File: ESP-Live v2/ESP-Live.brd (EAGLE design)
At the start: 64.8 x 30.5 mm, 34 parts, among them CN1 USBSMD, IC2 AP2210K-3.3TRG1, IC3 ESP-12F, Y1 RESONATORSMD

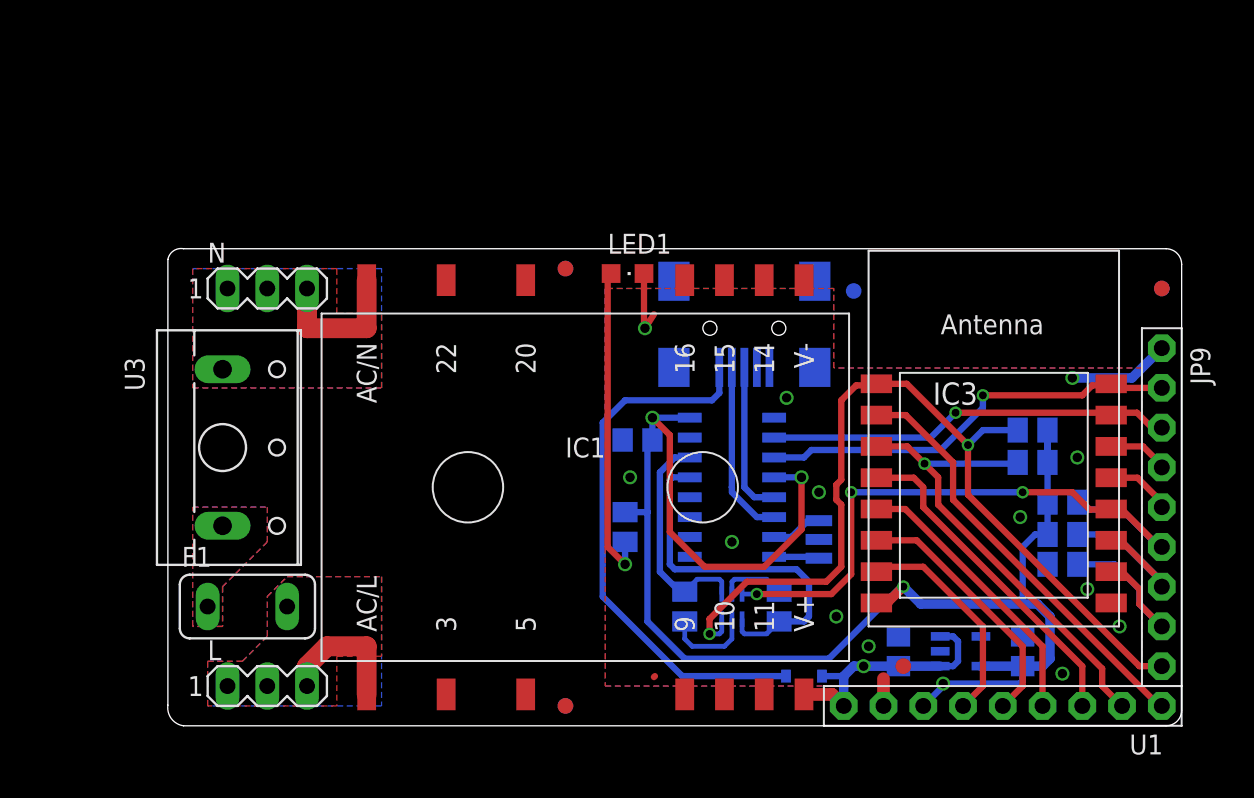
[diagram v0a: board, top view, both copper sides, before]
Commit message: with batery charger
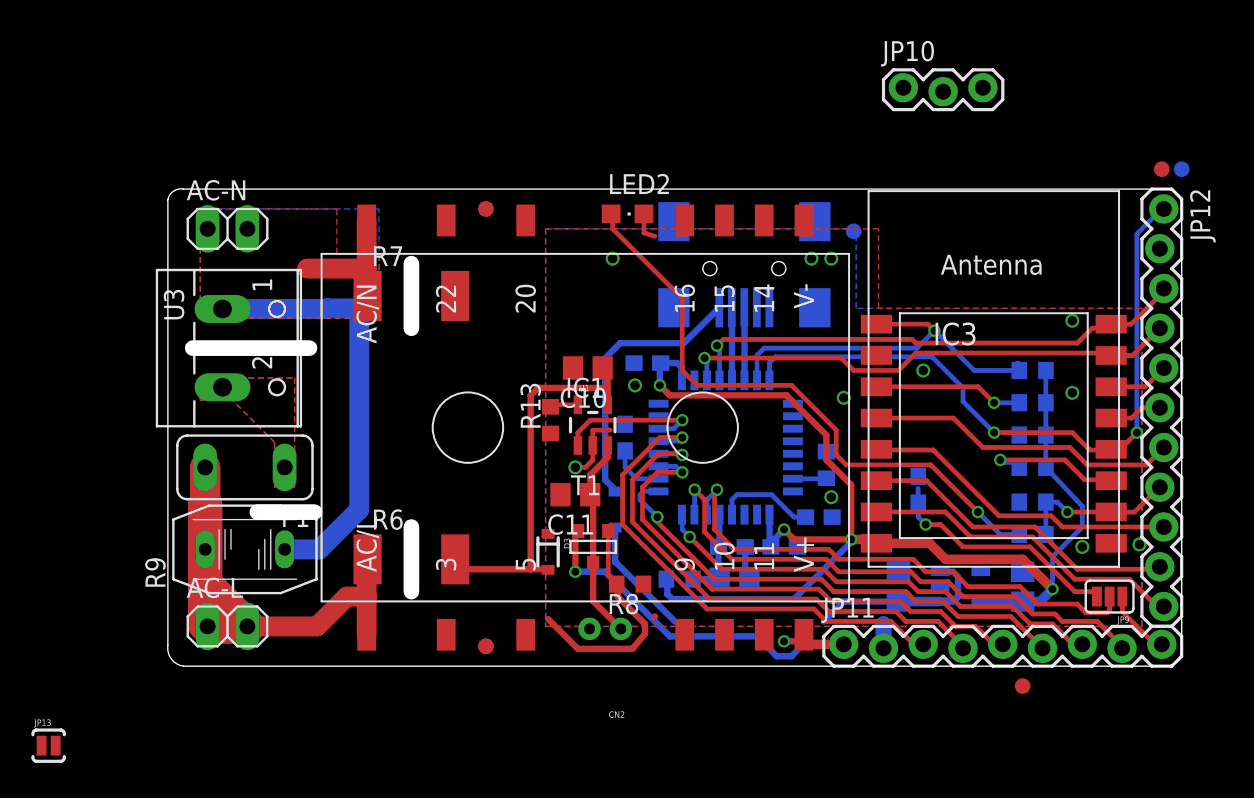
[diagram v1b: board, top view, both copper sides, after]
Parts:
- removed L, N: (no value), con-lstb:MA03-1
- removed LED1: (no value), adafruit:CHIPLED_0805
- removed U$2: MMDT3904, SparkFun:SOT363
- removed Y1: RESONATORSMD, SparkFun:RESONATOR-SMD
- added AC-L, AC-N: (no value), pinhead:1X02
- added C10, C11: 4.7uF, rcl:C0805
- added C4, C5, C7, C8, C9: 100nF, rcl:C0603
- added C6: 1uF, rcl:C0805
- added CN2: (no value), SparkFun:JST-2-PTH-NS
- added D3: PMEG3010EJ, SparkFun:SOD-323
- added JP10: (no value), SparkFun:1X03_LOCK
- added JP11: M09LOCK, SparkFun:1X09_LOCK
- added JP12: M11LOCK, SparkFun:1X11_LOCK
- added JP13: (no value), SparkFun:SJ_2S-NO
- added LED2: (no value), adafruit:CHIPLED_0805
- added R10: BEAD, rcl:R0603
- added R11: 10k, rcl:R0603
- added R12: 1k, rcl:R0603
- added R13: 2k, rcl:R0603
- added R9: 275VAC, varistor:P593
- added T1: (no value), zetex:SOT-23
- C3: value 0.1uF -> 100nF; device rcl:C0805 -> rcl:C0603
- JP9: value (none) -> CH1_CAP; device adafruit:1X09-BIG -> SparkFun:SJ_3_PASTE1&2
- R1, R2, R3, R4, R5: device rcl:M0805 -> rcl:R0603
- R6, R7: value 10k -> 0*; device rcl:M0805 -> rcl:R2512
- R8: value 1k -> 100k; device rcl:M0805 -> rcl:R0603
- U$1: value CH340G -> STM32F042K; device usb-serial:SOIC16 -> stm32:LQFP32
- U1: value (none) -> MCP73831; device adafruit:1X09-BIG -> SparkFun:SOT23-5
- U3: device con-wago-500:W237-113 -> con-wago-500:W237-102
- moved U1 31.7 mm to (27.1, 19.2), turned to 0 degrees
- moved R7 26.4 mm to (15.6, 27.5), flipped to the top, turned to 0 degrees
- moved R6 23.7 mm to (15.6, 10.6), flipped to the top, turned to 0 degrees
- moved D1 16.1 mm to (28.6, 13.8), turned to 90 degrees
- moved C3 11.6 mm to (39.4, 11.4), turned to 180 degrees
- moved F1 8.89 mm to (4.92, 16.5), turned to 180 degrees
- moved JP5 7.73 mm to (64.8, 35.6)
- moved JP4 7.73 mm to (54.6, 2.54)
- moved JP3 7.62 mm to (63.5, 35.6)
- moved JP9 6.62 mm to (60.2, 8.26), turned to 180 degrees
- moved JP2 6.35 mm to (20.3, 33.0)
- moved JP6 6.35 mm to (20.3, 33.0)
- moved JP1 6.35 mm to (20.3, 5.08)
- moved JP8 6.35 mm to (20.3, 5.08)
- moved U3 6.35 mm to (4.76, 24.1)
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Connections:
- removed net N$15: R7.1, U$1.14, U$2.1
- removed net N$16: CN1.D-, U$1.6
- removed net N$21: U$1.7, Y1.1
- removed net N$22: U$1.8, Y1.3
- removed net N$4: LED1.A, R8.2
- removed net N$8: R7.2, U$2.5
- new net BATT_STAT: U$1.14, U1.1
- new net BOOT0: JP10.3, R11.1, U$1.31
- new net L: AC-L.1, AC-L.2, F1.2, IC1.AC/L, R6.1, R9.1
- new net N: AC-N.1, AC-N.2, IC1.AC/N, R7.1, R9.2, U3.1
- new net N$13: C11.1, CN2.1, T1.1, U1.3
- new net N$6: CN1.D-, U$1.21
- new net N$7: CN1.D+, U$1.22
- new net SPI1_MISO: JP11.4, U$1.12
- new net SPI1_MOSI: JP11.3, U$1.13
- new net SPI1_SCK: JP11.5, U$1.11
- new net STM_NRST: C7.1, JP10.1, U$1.4
- new net TIM2_CH1: JP9.2, U$1.6
- new net TIM2_CH1_OPT: JP11.9, JP9.1
- new net TIM2_CH2: JP11.8, U$1.7
- new net TIM2_CH3: JP11.7, U$1.8
- new net TIM2_CH4: JP11.6, U$1.9
- new net V+: C1.1, D3.1, IC2.1, IC2.3, JP13.2, T1.2
- net +3V3: now also C4.1, JP10.2, R10.2, U$1.1, U$1.17; no longer R8.1, U$1.16, U$1.4, U1.7
- net +5V: now also C10.1, D3.2, JP11.1, JP13.1, R8.2, T1.3, U1.4; no longer C1.1, IC2.1, IC2.3, U1.9
- net ADC: no longer U1.1
- net CH_PD: no longer U1.2
- net GND: now also C10.2, C11.2, C4.2, C5.2, C6.2, C7.2, C8.2, C9.2, CN2.2, JP11.2, LED2.C, R11.2, R13.1, R7.2, R8.1, U$1.16, U$1.32, U1.2; no longer JP9.1, LED1.C, U$1.1, U1.8, Y1.2
- net GPIO0: now also JP12.1, U$1.24; no longer JP9.6, U$2.3
- net GPIO15: now also JP12.8, R12.1; no longer JP9.8
- net GPIO2: no longer JP9.7
- net IO12: now also JP12.10; no longer U1.5
- net IO13: now also JP12.11; no longer U1.6
- net IO14: now also JP12.9; no longer U1.4
- net IO16: now also JP12.7; no longer U1.3
- net IO4: now also JP12.6; no longer JP9.5
- net IO5: now also JP12.5; no longer JP9.4
- net N$10: now also LED2.A, R12.2; no longer R6.2, U$2.2
- net N$11: now also C9.1, U$1.10; no longer R6.1, U$1.13, U$2.4
- net N$12: now also C8.1, JP9.3; no longer CN1.D+, U$1.5
- net N$2: now also C5.1, C6.1, R10.1, U$1.5; no longer IC1.AC/N, N.1, N.2, N.3, U3.1
- net N$3: now also R13.2, U1.5; no longer F1.2, IC1.AC/L, L.1, L.2, L.3
- net RST: now also U$1.23; no longer JP9.9, U$2.6
- net RX: now also JP12.3, U$1.20; no longer JP9.2, U$1.3
- net TX: now also JP12.4, U$1.19; no longer JP9.3, U$1.2
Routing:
- net L: track 0.00 -> 46.8 mm
- net +5V: track 16.4 -> 52.0 mm
- net N$10: track 4.20 -> 38.7 mm, vias 0 -> 1
- net TIM2_CH2: track 0.00 -> 34.4 mm, vias 0 -> 1
- net N: track 0.00 -> 34.3 mm
- net RST: track 57.4 -> 24.3 mm, vias 2 -> 1
- net SPI1_SCK: track 0.00 -> 33.0 mm, vias 0 -> 1
- net TIM2_CH1: track 0.00 -> 32.8 mm, vias 0 -> 1
- net SPI1_MISO: track 0.00 -> 32.8 mm, vias 0 -> 1
- net SPI1_MOSI: track 0.00 -> 32.0 mm, vias 0 -> 1
- net TIM2_CH4: track 0.00 -> 31.6 mm, vias 0 -> 1
- net V+: track 0.00 -> 31.3 mm, vias 0 -> 1
- net TIM2_CH3: track 0.00 -> 29.6 mm, vias 0 -> 1
- net ADC: track 27.3 -> 0.00 mm
- net +3V3: track 102.7 -> 80.5 mm
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- added copper zone on layer 1, net N
- added copper zone on layer 16, net N
- removed copper zone on layer 1, net N$2
- removed copper zone on layer 16, net N$2
- removed copper zone on layer 1, net N$3
- removed copper zone on layer 16, net N$3
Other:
- outline, holes or cut-outs redrawn
- board text added: "BATTERY"
- board text added: "ESP-Live v2.0"
- board text added: "v2.0"
- board text removed: "CH340G"
- board text removed: "ESP-Live v1.0"
- board text removed: "v1.0"
